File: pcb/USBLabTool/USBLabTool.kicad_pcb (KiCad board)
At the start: 4 copper layers, 79.4 x 56.2 mm, 249 parts, among them J1 Conn_01x06_Pin, J17 2x01, J19 T_N5V, J2 Conn_02x12_Odd_Even, J20 USB_C_Receptacle, K1 G5V-2, K2 G5V-2, Q1 STL11N3LLH6, SW1 TS02-66-73-BK-100-SCR-D, U1 AQY284SX, U10 MC33274ADR2G, U11 DG403, U12 STM32H563VITx, U13 R1283K002A, U14 ST1L05APU33R, U15 ST1L05APU33R, U16 LTC1983ES6-5TRMPBF, U17 TCPP01-M12, U18 74HC245, U19 USBLC6-2SC6, U2 AQY284SX, U20 74HC245, U3 CD74HC4316, U4 LMP7718, U5 CD74HC4316, U6 LMP7718, U7 OPA863, U8 OPA863, U9 MC33274ADR2G, Y1 32.768kHz, Y2 NX2016SA-25M-EXS00A-CS08742

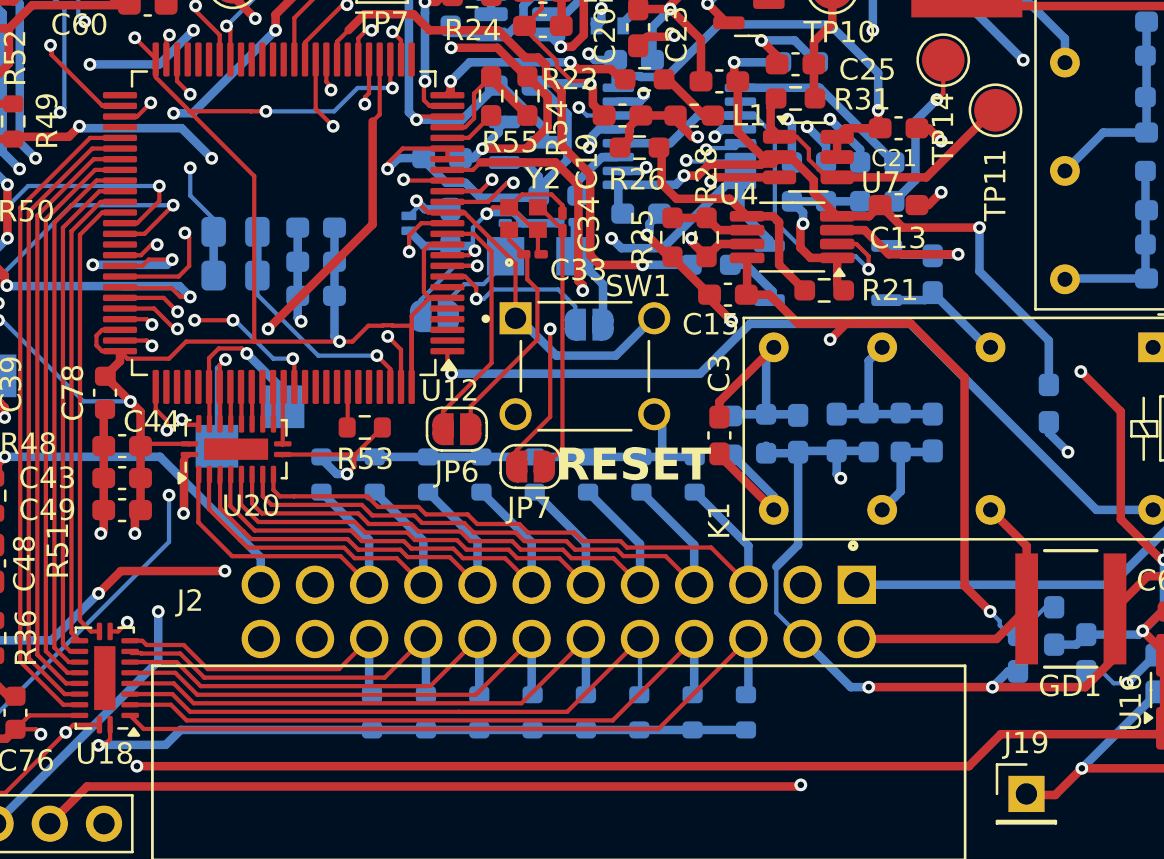
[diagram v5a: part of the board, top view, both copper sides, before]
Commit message: update PCB v2 caps
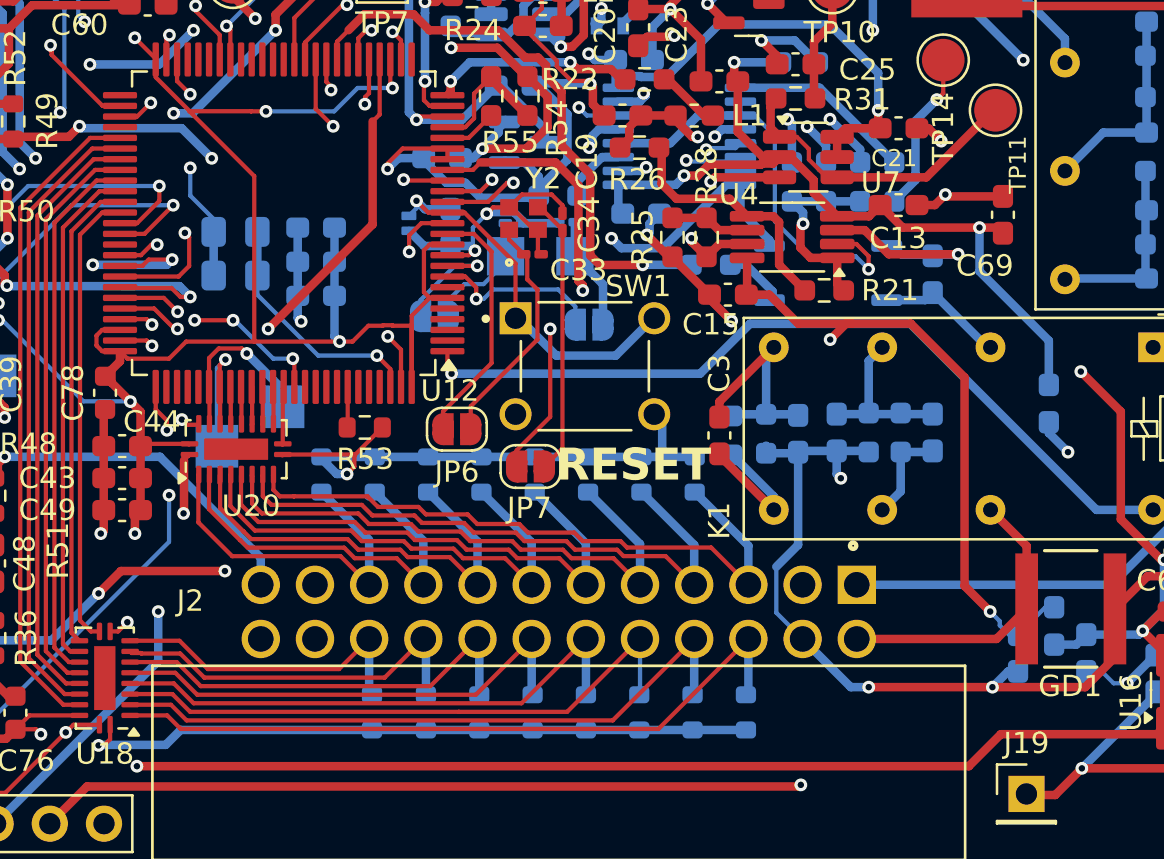
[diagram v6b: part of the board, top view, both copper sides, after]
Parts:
- added C69: 100n, Capacitor_SMD:C_0603_1608Metric_Pad1.08x0.95mm_HandSolder, F.Cu at (176.6, 90.9)
- C57: value 100n -> 10u
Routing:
- net GNDA: track 311.9 -> 314.8 mm
- net -5VCLEAN: track 108.2 -> 109.5 mm
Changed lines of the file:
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@@
 		)
 	)
+	(footprint "Capacitor_SMD:C_0603_1608Metric_Pad1.08x0.95mm_HandSolder"
+		(layer "F.Cu")
+		(at 176.6 90.9 90)
+		(descr "Capacitor SMD 0603 (1608 Metric), square (rectangular) end terminal, IPC-7351 nominal with elongated pad for handsoldering. (Body size source: IPC-SM-782 page 76, https://www.pcb-3d.com/wordpress/wp-content/uploads/ipc-sm-782a_amendment_1_and_2.pdf), generated with kicad-footprint-generator")
+		(tags "capacitor handsolder")
+		(property "Reference" "C69"
+			(at -2.3875 -0.85 180)
+			(layer "F.SilkS")
+			(effects
+				(font
+					(size 1 1)
+					(thickness 0.15)
+				)
+			)
+		)
+		(property "Value" "100n"
+			(at 0 1.43 90)
+			(layer "F.Fab")
+			(effects
+				(font
+					(size 1 1)
+					(thickness 0.15)
+				)
+			)
+		)
+		(property "Datasheet" ""
+			(at 0 0 90)
+			(layer "F.Fab")
+			(hide yes)
+			(effects
+				(font
+					(size 1.27 1.27)
+					(thickness 0.15)
+				)
+			)
+		)
+		(property "Description" ""
+			(at 0 0 90)
+			(layer "F.Fab")
+			(hide yes)
+			(effects
+				(font
+					(size 1.27 1.27)
+					(thickness 0.15)
+				)
+			)
+		)
+		(property ki_fp_filters "C_*")
+		(sheetname "/psu/")
+		(sheetfile "Power_Supply.kicad_sch")
+		(attr smd)
+		(fp_line
+			(start -0.146267 -0.51)
+			(end 0.146267 -0.51)
+			(stroke
+				(width 0.12)
+				(type solid)
+			)
+			(layer "F.SilkS")
+		)
+		(fp_line
+			(start -0.146267 0.51)
+			(end 0.146267 0.51)
+			(stroke
+				(width 0.12)
+				(type solid)
+			)
+			(layer "F.SilkS")
+		)
+		(fp_line
+			(start 1.65 -0.73)
+			(end 1.65 0.73)
+			(stroke
+				(width 0.05)
+				(type solid)
+			)
+			(layer "F.CrtYd")
+		)
+		(fp_line
+			(start -1.65 -0.73)
+			(end 1.65 -0.73)
+			(stroke
+				(width 0.05)
+				(type solid)
+			)
+			(layer "F.CrtYd")
+		)
+		(fp_line
+			(start 1.65 0.73)
+			(end -1.65 0.73)
+			(stroke
+				(width 0.05)
+				(type solid)
+			)
+			(layer "F.CrtYd")
+		)
+		(fp_line
+			(start -1.65 0.73)
+			(end -1.65 -0.73)
+			(stroke
+				(width 0.05)
+				(type solid)
+			)
+			(layer "F.CrtYd")
+		)
+		(fp_line
+			(start 0.8 -0.4)
+			(end 0.8 0.4)
+			(stroke
+				(width 0.1)
+				(type solid)
+			)
+			(layer "F.Fab")
+		)
+		(fp_line
+			(start -0.8 -0.4)
+			(end 0.8 -0.4)
+			(stroke
+				(width 0.1)
+				(type solid)
+			)
+			(layer "F.Fab")
+		)
+		(fp_line
+			(start 0.8 0.4)
+			(end -0.8 0.4)
+			(stroke
+				(width 0.1)
+				(type solid)
+			)
+			(layer "F.Fab")
+		)
+		(fp_line
+			(start -0.8 0.4)
+			(end -0.8 -0.4)
+			(stroke
+				(width 0.1)
+				(type solid)
+			)
+			(layer "F.Fab")
+		)
+		(fp_text user "${REFERENCE}"
+			(at 0 0 90)
+			(layer "F.Fab")
+			(effects
+				(font
+					(size 0.4 0.4)
+					(thickness 0.06)
+				)
+			)
+		)
+		(pad "1" smd roundrect
+			(at -0.8625 0 90)
+			(size 1.075 0.95)
+			(layers "F.Cu" "F.Mask" "F.Paste")
+			(roundrect_rratio 0.25)
+			(net 18 "-5VCLEAN")
+			(pintype "passive")
+		)
+		(pad "2" smd roundrect
+			(at 0.8625 0 90)
+			(size 1.075 0.95)
+			(layers "F.Cu" "F.Mask" "F.Paste")
+			(roundrect_rratio 0.25)
+			(net 2 "GNDA")
+			(pintype "passive")
+		)
+		(embedded_fonts no)
+		(model "${KICAD9_3DMODEL_DIR}/Capacitor_SMD.3dshapes/C_0603_1608Metric.wrl"
+			(offset
+				(xyz 0 0 0)
+			)
+			(scale
+				(xyz 1 1 1)
+			)
+			(rotate
+				(xyz 0 0 0)
+			)
+		)
+	)
 	(footprint "Capacitor_SMD:C_0201_0603Metric_Pad0.64x0.40mm_HandSolder"
 		(layer "F.Cu")
@@
 		(tags "test point SMD pad")
 		(property "Reference" "TP11"
-			(at 0 3.5 90)
+			(at 1.05 2.55 90)
 			(layer "F.SilkS")
 			(effects
 				(font
-					(size 1 1)
+					(size 0.8 0.8)
 					(thickness 0.15)
 				)
@@
 			)
 		)
-		(property "Value" "100n"
+		(property "Value" "10u"
 			(at 0 -1.43 0)
 			(layer "B.Fab")
@@
 	)
 	(segment
+		(start 173.406 90.444)
+		(end 173.9 89.95)
+		(width 0.4)
+		(layer "F.Cu")
+		(net 2)
+	)
+	(segment
 		(start 150.556 87.794)
 		(end 150.556 88.294)
@@
 	)
 	(segment
+		(start 176.6 90.0375)
+		(end 173.9875 90.0375)
+		(width 0.4)
+		(layer "F.Cu")
+		(net 2)
+	)
+	(segment
 		(start 131.089 81.075)
 		(end 135.6125 81.075)
@@
 	)
 	(segment
+		(start 172.5685 90.444)
+		(end 173.406 90.444)
+		(width 0.4)
+		(layer "F.Cu")
+		(net 2)
+	)
+	(segment
 		(start 159.504625 81.254625)
 		(end 159.5 81.25)
@@
 	)
 	(segment
-		(start 172.5685 90.444)
-		(end 173.106 90.444)
-		(width 0.4)
-		(layer "F.Cu")
-		(net 2)
-	)
-	(segment
 		(start 122.75 104.725)
 		(end 122.75 105.5)
@@
 	)
 	(segment
-		(start 173.106 90.444)
-		(end 173.706 89.844)
-		(width 0.4)
-		(layer "F.Cu")
-		(net 2)
-	)
-	(segment
 		(start 174.906 76.9739)
 		(end 175.7761 76.9739)
@@
 	)
 	(segment
+		(start 173.9875 90.0375)
+		(end 173.9 89.95)
+		(width 0.4)
+		(layer "F.Cu")
+		(net 2)
+	)
+	(segment
 		(start 130 82.164)
 		(end 130 83.809999)
@@
 	)
 	(via
+		(at 173.9 89.95)
+		(size 0.6)
+		(drill 0.3)
+		(layers "F.Cu" "B.Cu")
+		(net 2)
+	)
+	(via
 		(at 169 103.25)
 		(size 0.6)
@@
 	)
 	(via
-		(at 173.706 89.844)
-		(size 0.6)
-		(drill 0.3)
-		(layers "F.Cu" "B.Cu")
-		(net 2)
-	)
-	(via
 		(at 126.475 84.55)
 		(size 0.6)
@@
 	)
 	(segment
+		(start 175.5 91.5)
+		(end 176.3375 91.5)
+		(width 0.4)
+		(layer "F.Cu")
+		(net 18)
+	)
+	(segment
 		(start 150.6375 78.648)
 		(end 149.351 77.3615)
@@
 	)
 	(segment
+		(start 176.3375 91.5)
+		(end 176.6 91.7625)
+		(width 0.4)
+		(layer "F.Cu")
+		(net 18)
+	)
+	(segment
 		(start 164 83.75)
 		(end 164 84.4755)
@@
 	)
 	(segment
-		(start 136.45 111.067)
-		(end 138.1961 111.067)
-		(width 0.2)
-		(layer "F.Cu")
-		(net 58)
-	)
-	(segment
-		(start 136.252 110.869)
-		(end 136.45 111.067)
+		(start 139.3251 112.196)
+		(end 145.474 112.196)
 		(width 0.2)
 		(layer "F.Cu")
@@
 	)
 	(segment
-		(start 145.474 112.196)
-		(end 146.886 110.784)
+		(start 135.681 110.869)
+		(end 137.9981 110.869)
 		(width 0.2)
 		(layer "F.Cu")
@@
 	)
 	(segment
-		(start 138.1961 111.067)
+		(start 137.9981 110.869)
 		(end 139.3251 112.196)
 		(width 0.2)
@@
 	)
 	(segment
-		(start 135.681 110.869)
-		(end 136.252 110.869)
-		(width 0.2)
-		(layer "F.Cu")
-		(net 58)
-	)
-	(segment
-		(start 139.3251 112.196)
-		(end 145.474 112.196)
+		(start 145.474 112.196)
+		(end 146.886 110.784)
 		(width 0.2)
 		(layer "F.Cu")
@@
 	)
 	(segment
-		(start 136.315 115.003)
+		(start 138.053 115.003)
 		(end 160.447 115.003)
 		(width 0.2)
@@
 	)
 	(segment
+		(start 137.419 114.369)
+		(end 138.053 115.003)
+		(width 0.2)
+		(layer "F.Cu")
+		(net 65)
+	)
+	(segment
 		(start 135.681 114.369)
-		(end 136.315 115.003)
+		(end 137.419 114.369)
 		(width 0.2)
 		(layer "F.Cu")

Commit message: update pcb v2
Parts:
- moved C69 2.06 mm to (175.3, 89.3)
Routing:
- net GNDA: track 314.8 -> 314.2 mm
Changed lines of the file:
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@@
 	(footprint "Capacitor_SMD:C_0603_1608Metric_Pad1.08x0.95mm_HandSolder"
 		(layer "F.Cu")
-		(at 176.6 90.9 90)
+		(at 175.35 89.2625 90)
 		(descr "Capacitor SMD 0603 (1608 Metric), square (rectangular) end terminal, IPC-7351 nominal with elongated pad for handsoldering. (Body size source: IPC-SM-782 page 76, https://www.pcb-3d.com/wordpress/wp-content/uploads/ipc-sm-782a_amendment_1_and_2.pdf), generated with kicad-footprint-generator")
 		(tags "capacitor handsolder")
 		(property "Reference" "C69"
-			(at -2.3875 -0.85 180)
+			(at -3.1375 0.65 270)
 			(layer "F.SilkS")
 			(effects
@@
 		(tags "capacitor handsolder")
 		(property "Reference" "C21"
-			(at 0.206 -1.406 180)
+			(at 0.506 -1.206 180)
 			(layer "F.SilkS")
 			(effects
@@
 	)
 	(segment
-		(start 176.6 90.0375)
-		(end 173.9875 90.0375)
-		(width 0.4)
-		(layer "F.Cu")
-		(net 2)
-	)
-	(segment
 		(start 131.089 81.075)
 		(end 135.6125 81.075)
@@
 	)
 	(segment
+		(start 173.9 89.85)
+		(end 175.35 88.4)
+		(width 0.4)
+		(layer "F.Cu")
+		(net 2)
+	)
+	(segment
 		(start 123.015 105.515)
 		(end 124.225 105.515)
@@
 	)
 	(segment
+		(start 173.9 89.95)
+		(end 173.9 89.85)
+		(width 0.4)
+		(layer "F.Cu")
+		(net 2)
+	)
+	(segment
 		(start 174.906 76.9739)
 		(end 175.7761 76.9739)
@@
 	)
 	(segment
-		(start 173.9875 90.0375)
-		(end 173.9 89.95)
-		(width 0.4)
-		(layer "F.Cu")
-		(net 2)
-	)
-	(segment
 		(start 130 82.164)
 		(end 130 83.809999)
@@
 	)
 	(segment
-		(start 175.5 91.5)
-		(end 176.3375 91.5)
+		(start 150.6375 78.648)
+		(end 149.351 77.3615)
 		(width 0.4)
 		(layer "F.Cu")
@@
 	)
 	(segment
-		(start 150.6375 78.648)
-		(end 149.351 77.3615)
+		(start 168.831 90.969)
+		(end 170.3185 90.969)
 		(width 0.4)
 		(layer "F.Cu")
@@
 	)
 	(segment
-		(start 168.831 90.969)
-		(end 170.3185 90.969)
+		(start 175.5 90.275)
+		(end 175.35 90.125)
 		(width 0.4)
 		(layer "F.Cu")
@@
 	)
 	(segment
-		(start 176.3375 91.5)
-		(end 176.6 91.7625)
-		(width 0.4)
-		(layer "F.Cu")
-		(net 18)
-	)
-	(segment
 		(start 164 83.75)
 		(end 164 84.4755)
@@
 		(width 0.4)
 		(layer "F.Cu")
+		(net 18)
+	)
+	(segment
+		(start 175.5 91.5)
+		(end 175.5 90.275)
+		(width 0.4)
+		(layer "F.Cu")
